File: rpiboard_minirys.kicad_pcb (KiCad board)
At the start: 4 copper layers, 65 x 56 mm, 128 parts, among them IC1 LM51231QRGRRQ1, IC2 TPS564242DRLR, IC3 L6470H, IC4 L6470H, IC5 74AUP2G00DC,125, IC6 MAX11613EUA+T, J1 RPi_GPIO, J10 ToF1_Sensor, J11 ToF2_Sensor, J12 ToF3_Sensor, J13 ToF4_Sensor, J14 ToF5_Sensor, J15 ToF6_Sensor, J16 SPI_Connector, J17 UART_Connector, J18 Fan_Connector, J2 Motor_L, J3 Motor_R, J4 B_Cell_3, J5 B_Cell_2, J6 B_Cell_1, J7 SW, J8 Temp_Sensor, J9 IMU_Sensor, Q1 DMG1012T-7, Q2 ISZ065N03L5S, Q3 ISZ065N03L5S, Q4 DMG1012T-7, Q5 DMG1012T-7, Q6 DMG1012T-7

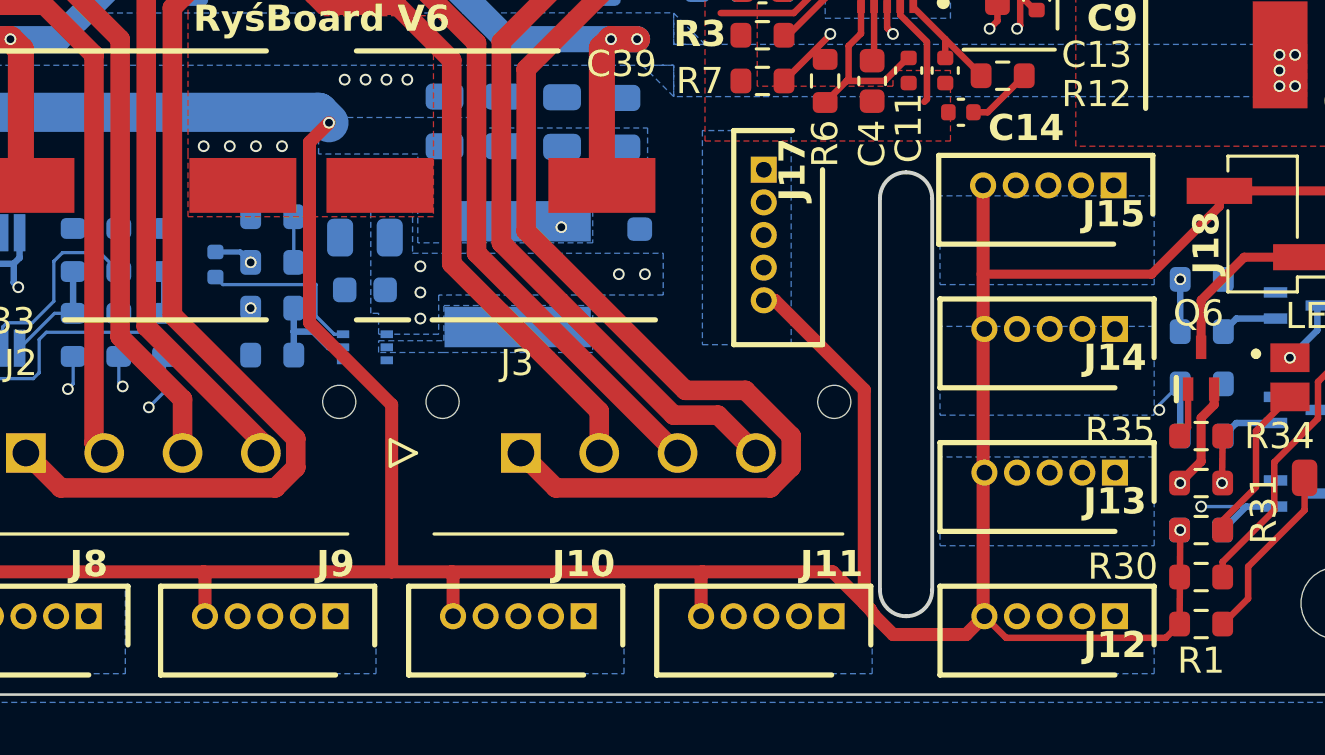
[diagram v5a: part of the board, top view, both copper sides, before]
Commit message: Adjusted south connectors position
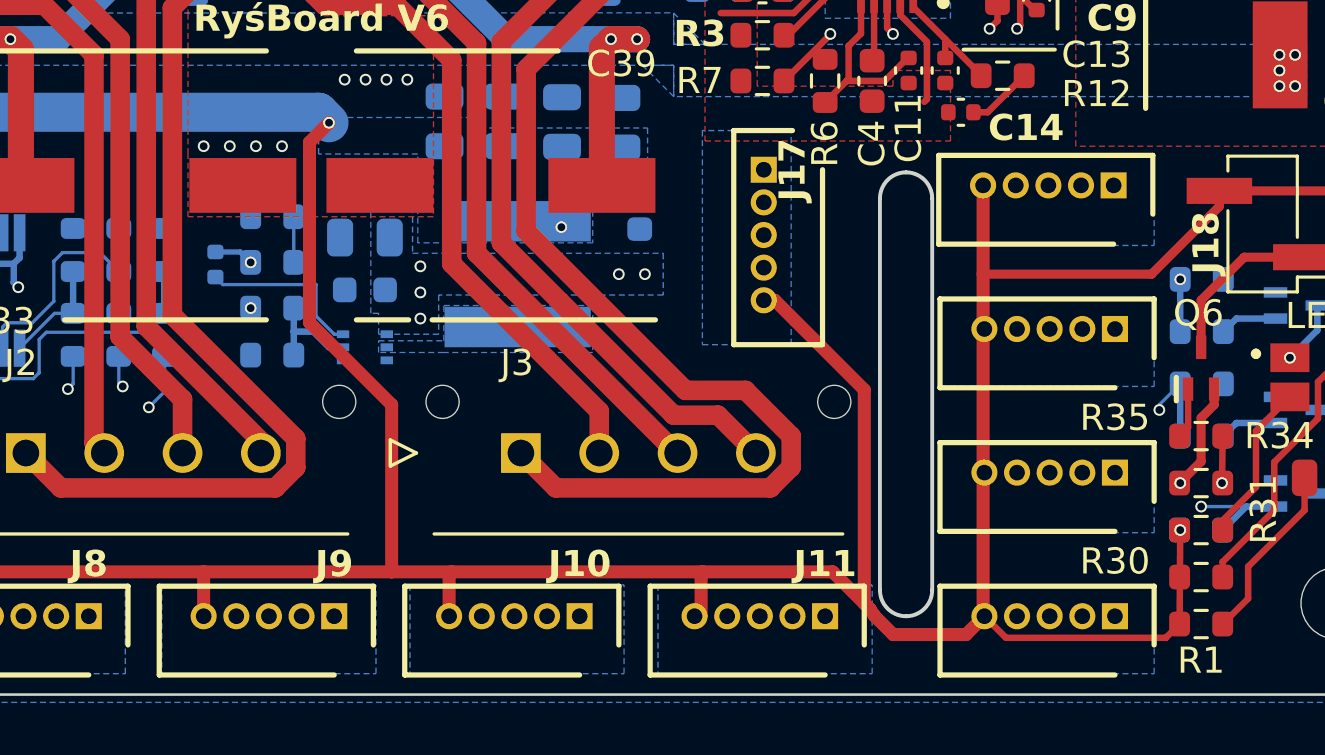
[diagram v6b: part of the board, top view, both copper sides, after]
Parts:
- moved J11 0.25 mm to (63.4, 74.5)
- moved J10 0.15 mm to (54.0, 74.5)

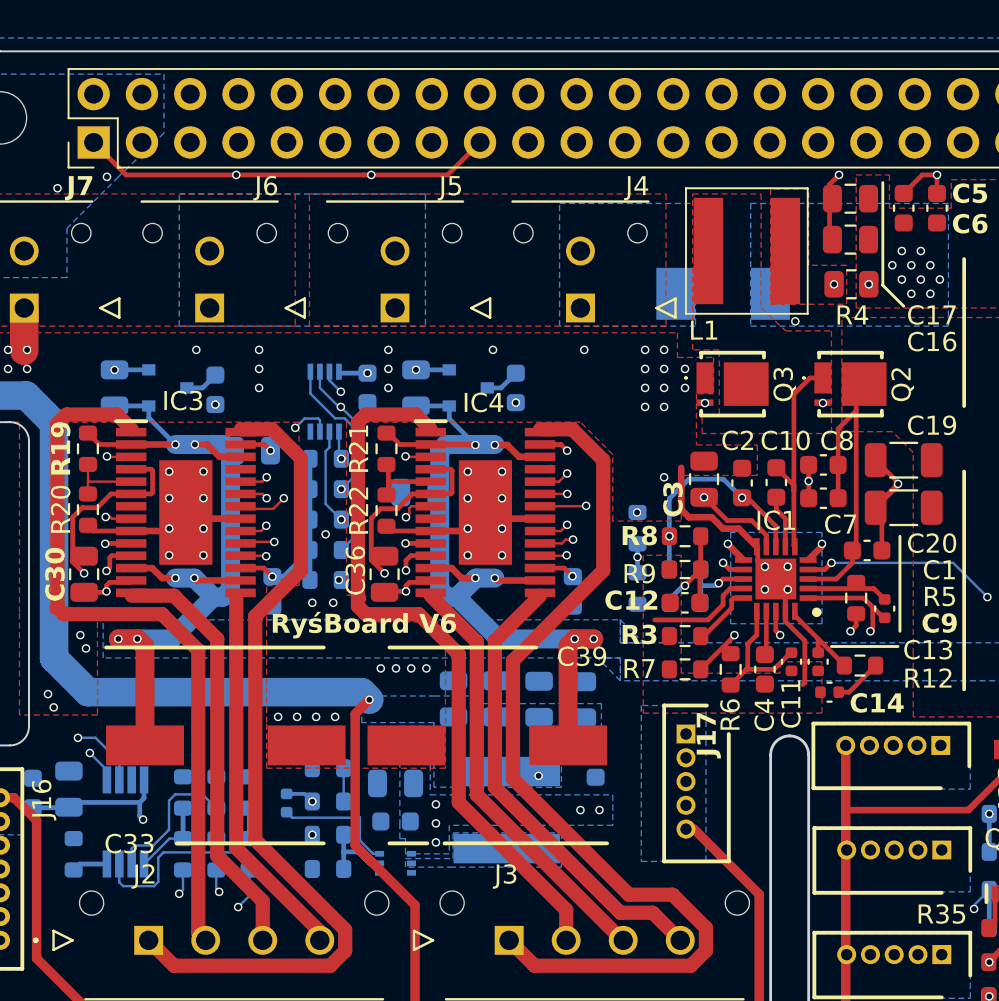
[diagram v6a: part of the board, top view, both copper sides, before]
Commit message: Minimized empty space in copper pour
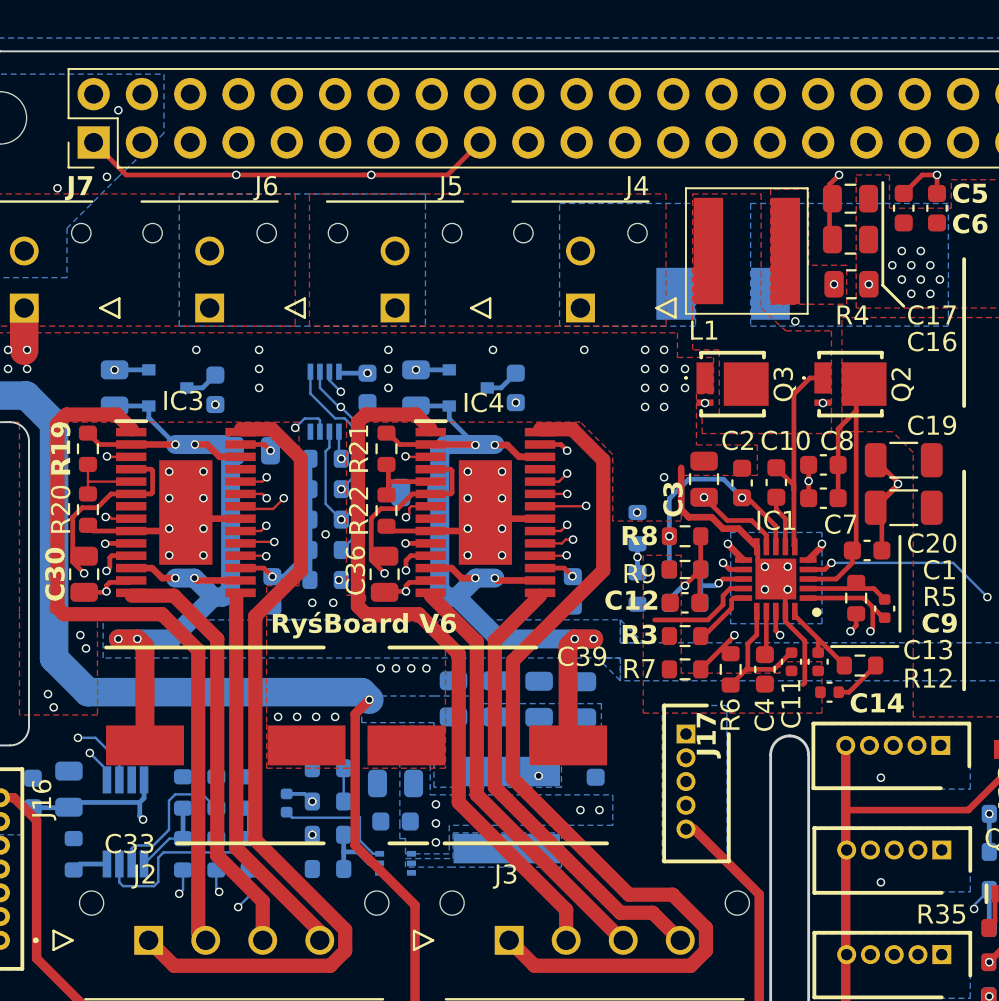
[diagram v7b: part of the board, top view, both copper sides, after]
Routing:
- net /Connectors/TOF1_EN: track 40.4 -> 73.5 mm
- net /Connectors/I2C3_SCL: track 123.9 -> 154.4 mm
- net /Connectors/TOF2_EN: track 38.9 -> 63.0 mm
- net /Connectors/I2C3_SDA: track 82.6 -> 105.2 mm
- net /Connectors/I2C5_SDA: track 39.1 -> 61.3 mm
- net /Connectors/TOF3_EN: track 36.6 -> 58.1 mm
- net /Connectors/I2C5_SCL: track 36.0 -> 56.5 mm
- net /Connectors/TOF4_EN: track 37.2 -> 53.4 mm
- net /Connectors/TOF5_EN: track 32.1 -> 41.9 mm
- net /Connectors/SPI_IRQ: track 69.7 -> 65.5 mm
- net /Connectors/CELL_1: track 42.3 -> 44.7 mm
- net /Connectors/TOF6_EN: track 31.7 -> 33.6 mm
- net /Connectors/UART_TX: track 70.3 -> 68.8 mm
- net +3.3V: track 158.6 -> 159.3 mm
- net /Connectors/SPI_MOSI: track 60.3 -> 61.0 mm
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
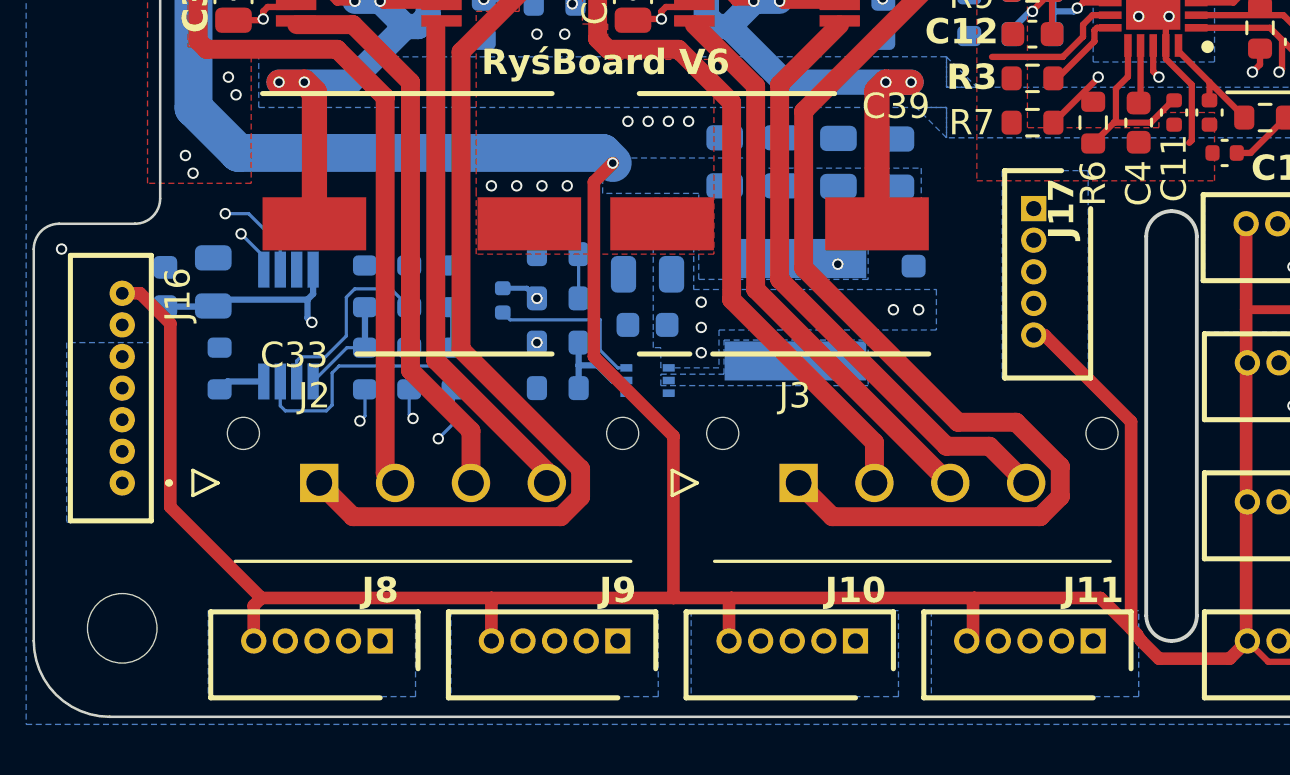
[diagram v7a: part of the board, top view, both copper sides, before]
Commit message: Fixed reference designators positioning
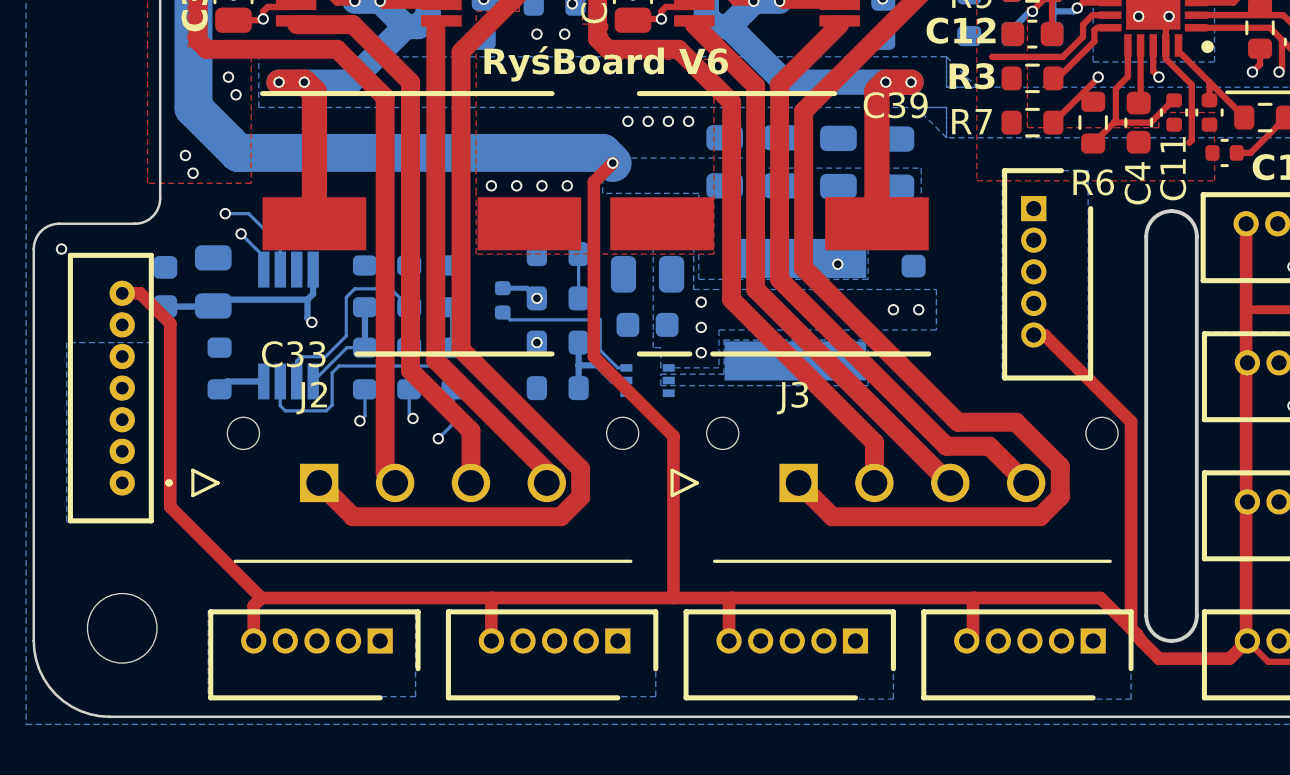
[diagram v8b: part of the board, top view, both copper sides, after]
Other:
- board text added: "SN: JLCJLCJLCJLC"
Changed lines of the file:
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@@
     (property "ki_keywords" "connector")
     (attr through_hole)
-    (fp_text reference "J11" (at 0 -2) (layer "F.SilkS")
-        (effects (font (size 1 1) (thickness 0.2) bold))
+    (fp_text reference "J11" (at -5 1.5) (layer "B.SilkS")
+        (effects (font (size 1 1) (thickness 0.2) bold) (justify mirror))
     )
     (fp_text value "ToF2_Sensor" (at 0 1.1) (layer "F.SilkS") hide
@@
     (property "ki_keywords" "connector")
     (attr through_hole)
-    (fp_text reference "J8" (at 0 -2) (layer "F.SilkS")
-        (effects (font (size 1 1) (thickness 0.2) bold))
+    (fp_text reference "J8" (at -5 1.5) (layer "B.SilkS")
+        (effects (font (size 1 1) (thickness 0.2) bold) (justify mirror))
     )
     (fp_text value "Temp_Sensor" (at 0 1.05) (layer "F.SilkS") hide
@@
     (property "ki_keywords" "connector")
     (attr through_hole)
-    (fp_text reference "J10" (at 0 -2) (layer "F.SilkS")
-        (effects (font (size 1 1) (thickness 0.2) bold))
+    (fp_text reference "J10" (at -5 1.5) (layer "B.SilkS")
+        (effects (font (size 1 1) (thickness 0.2) bold) (justify mirror))
     )
     (fp_text value "ToF1_Sensor" (at 0 1.1) (layer "F.SilkS") hide
@@
     (property "ki_keywords" "R res resistor")
     (attr smd)
-    (fp_text reference "R6" (at -2.4 0 270) (layer "F.SilkS")
+    (fp_text reference "R6" (at -2.4 0) (layer "F.SilkS")
         (effects (font (size 1 1) (thickness 0.2)))
     )
@@
     (property "ki_keywords" "connector")
     (attr through_hole)
-    (fp_text reference "J17" (at 0 1.1 90) (layer "F.SilkS")
-        (effects (font (size 1 1) (thickness 0.2) bold))
+    (fp_text reference "J17" (at -5 1.55 90) (layer "B.SilkS")
+        (effects (font (size 1 1) (thickness 0.2) bold) (justify mirror))
     )
     (fp_text value "UART_Connector" (at 0 1.1 90) (layer "F.SilkS") hide
@@
     (property "ki_keywords" "connector")
     (attr through_hole)
-    (fp_text reference "J16" (at -7.45 -2.2 90) (layer "F.SilkS")
-        (effects (font (size 1 1) (thickness 0.2)))
+    (fp_text reference "J16" (at -5.85 1.4 90) (layer "B.SilkS")
+        (effects (font (size 1 1) (thickness 0.2)) (justify mirror))
     )
     (fp_text value "SPI_Connector" (at -3.75 0.075 90) (layer "F.SilkS") hide
@@
     (property "ki_keywords" "connector")
     (attr through_hole)
-    (fp_text reference "J9" (at 0 -2) (layer "F.SilkS")
-        (effects (font (size 1 1) (thickness 0.2) bold))
+    (fp_text reference "J9" (at -5 1.5) (layer "B.SilkS")
+        (effects (font (size 1 1) (thickness 0.2) bold) (justify mirror))
     )
     (fp_text value "IMU_Sensor" (at 0 1.1) (layer "F.SilkS") hide
@@
   (gr_arc locked (start 22.5 41) (mid 21.792893 40.707107) (end 21.5 40)
     (stroke (width 0.1) (type default)) (layer "Edge.Cuts"))
+  (gr_text "SN: JLCJLCJLCJLC" (at 76.5 43.5 -90) (layer "B.SilkS")
+    (effects (font (size 1 1) (thickness 0.2) bold) (justify left bottom mirror))
+  )
   (gr_text "10A" (at 64.6 32.4) (layer "B.SilkS")
     (effects (font (size 1 1) (thickness 0.2) bold) (justify left bottom mirror))
@@
     (effects (font (size 1 1) (thickness 0.2) bold) (justify left bottom))
   )
-  (gr_text_box "Designer: Kamil Adam Jabłoński\nWarsaw University of Technology\n\nRevision: 1.0 / 25.03.2024\nSN: JLCJLCJLCJLC"
+  (gr_text_box "Designer: Kamil Adam Jabłoński\nWarsaw University of Technology\n\nRevision: 1.0 / 25.03.2024"
     (start 85.4 29.675) (end 76.3 56.325) (angle 270) (layer "B.SilkS")
       (effects (font (size 1 1) (thickness 0.2) bold) (justify left top mirror))
@@
     (polygon
       (pts
-        (xy 47.5 73.3)
-        (xy 47.5 76.7)
-        (xy 55.7 76.7)
-        (xy 55.7 73.3)
+        (xy 47.3 73.4)
+        (xy 47.3 76.8)
+        (xy 55.5 76.8)
+        (xy 55.5 73.4)
       )
     )
@@
     (polygon
       (pts
-        (xy 38 73.3)
-        (xy 38 76.7)
-        (xy 46.2 76.7)
-        (xy 46.2 73.3)
+        (xy 37.9 73.3)
+        (xy 37.9 76.7)
+        (xy 46.1 76.7)
+        (xy 46.1 73.3)
       )
     )
@@
     (polygon
       (pts
-        (xy 57 73.3)
-        (xy 57 76.7)
-        (xy 65.2 76.7)
-        (xy 65.2 73.3)
+        (xy 56.7 73.4)
+        (xy 56.7 76.8)
+        (xy 64.9 76.8)
+        (xy 64.9 73.4)
       )
     )
